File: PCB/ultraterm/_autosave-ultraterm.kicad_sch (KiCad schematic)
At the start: 13 parts, among them J1 ILI9341, J2 Battery_plug, J3 SD_Card_Receptacle, J4 SD_Card_Device, J5 Micro_SD_Card, SW1 SW_Push, SW2 SW_Push, SW3 SW_Push, SW4 SW_SPST, U2 LM809

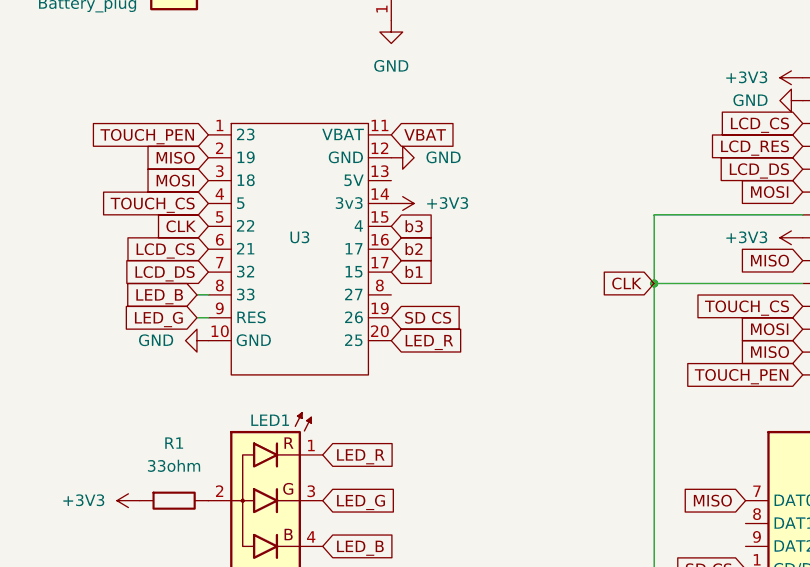
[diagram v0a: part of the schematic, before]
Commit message: playlist, skipping, pause all functional
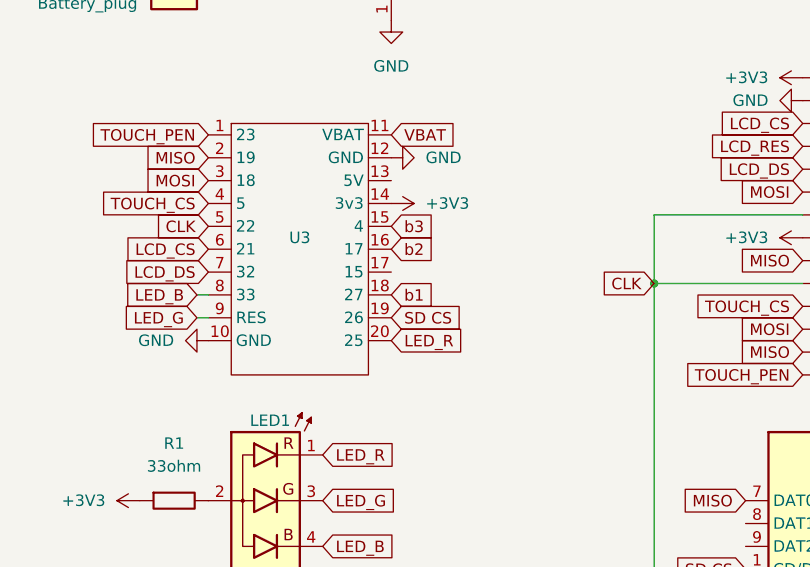
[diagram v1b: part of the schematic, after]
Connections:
- net b1: now also U3.18 (27); no longer U3.17 (15)
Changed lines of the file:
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@@
+		)
+	)
+	(global_label "b1"
+		(shape input)
+		(at 66.04 71.12 0)
+		(fields_autoplaced yes)
+		(effects
+			(font
+				(size 1.27 1.27)
+			)
+			(justify left)
+		)
+		(property "Intersheetrefs" "${INTERSHEET_REFS}"
+			(at 71.3837 71.12 0)
+			(effects
+				(font
+					(size 1.27 1.27)
+				)
+				(justify left)
+				(hide yes)
+			)
 		)
 	)
@@
 				)
 				(justify right)
-				(hide yes)
-			)
-		)
-	)
-	(global_label "b1"
-		(shape input)
-		(at 66.04 68.58 0)
-		(fields_autoplaced yes)
-		(effects
-			(font
-				(size 1.27 1.27)
-			)
-			(justify left)
-		)
-		(property "Intersheetrefs" "${INTERSHEET_REFS}"
-			(at 71.3837 68.58 0)
-			(effects
-				(font
-					(size 1.27 1.27)
-				)
-				(justify left)
 				(hide yes)
 			)
@@
 		(pin "9"
 		)
-		(pin "8"
+		(pin "18"
 		)
 		(pin "3"
